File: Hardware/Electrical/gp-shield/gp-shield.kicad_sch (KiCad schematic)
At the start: 0 parts

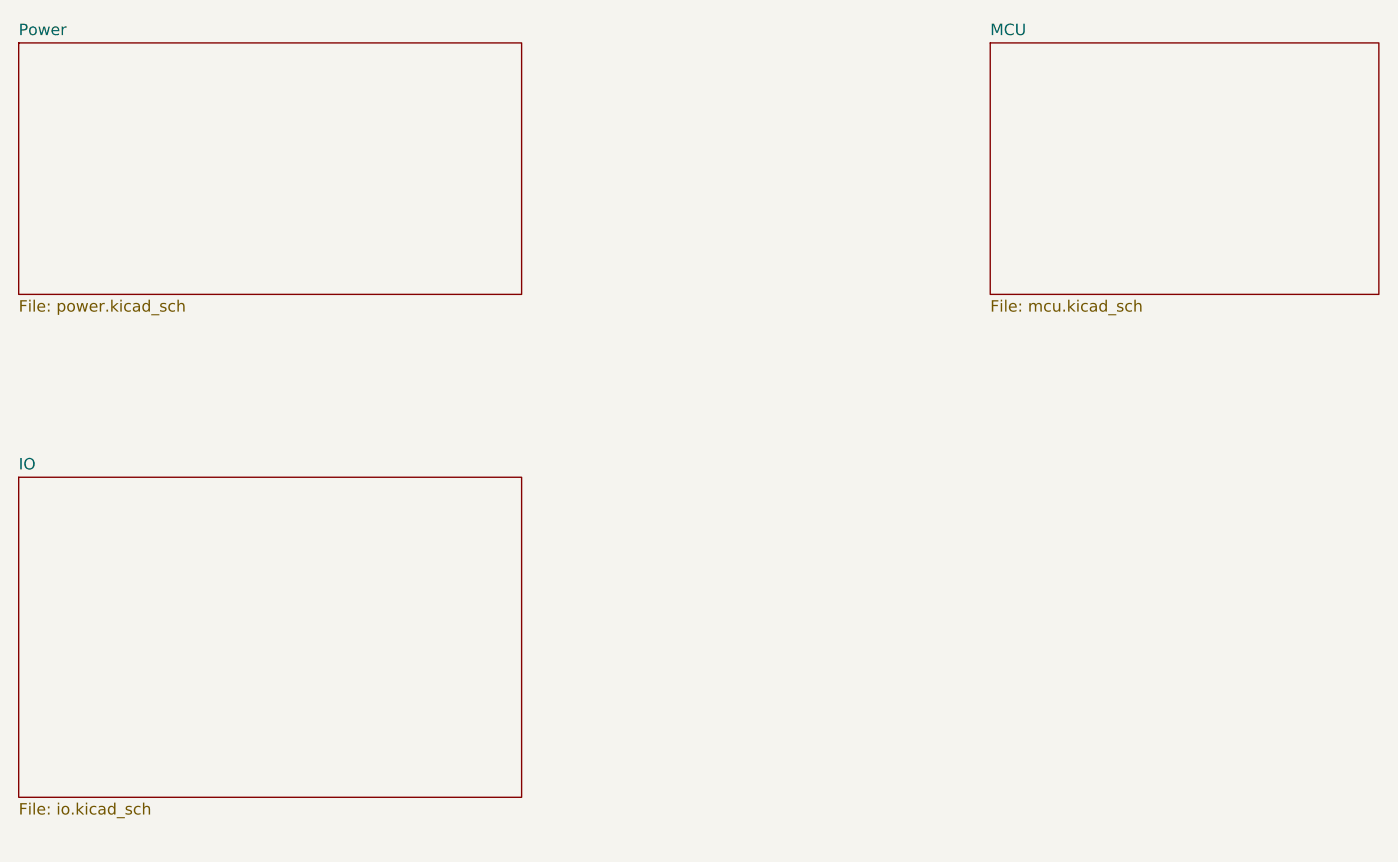
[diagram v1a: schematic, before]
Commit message: Major revisions to PCB layout
- near final layout
- prototype version of silkscreen
- removed 3.3V reg
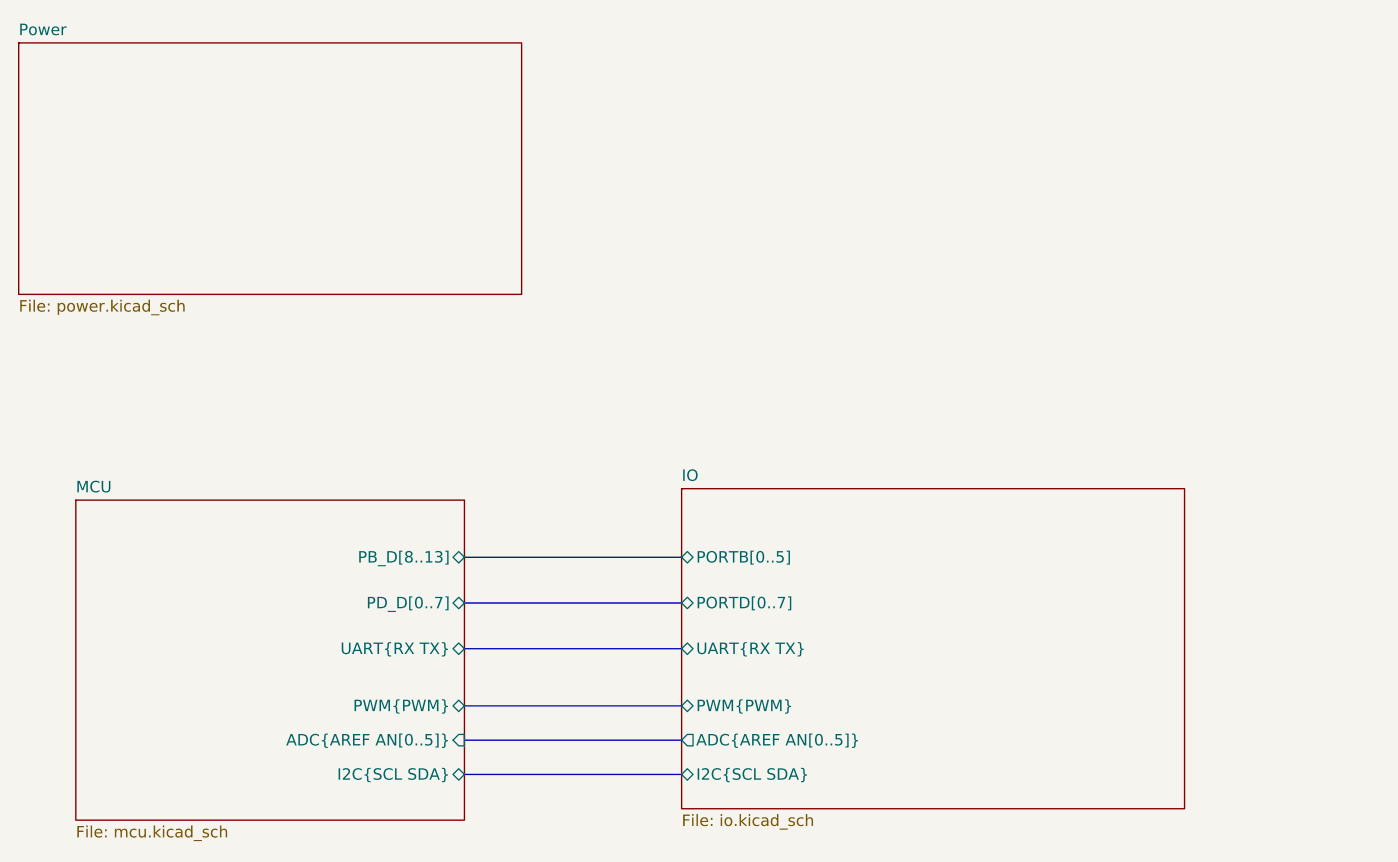
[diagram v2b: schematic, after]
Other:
- sheet IO ports: added ADC{AREF AN[0..5]}, I2C{SCL SDA}, PORTB[0..5], PORTD[0..7], PWM{PWM}, UART{RX TX}; removed none
- sheet MCU ports: added ADC{AREF AN[0..5]}, I2C{SCL SDA}, PB_D[8..13], PD_D[0..7], PWM{PWM}, UART{RX TX}; removed none
